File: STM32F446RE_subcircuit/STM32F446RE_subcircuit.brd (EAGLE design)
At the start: 88.6 x 55.9 mm, 47 parts, among them IC1 74AC126N, IC2 LD117AS33TR, IC3 74AC126N, IC4 74HC04N, IC5 74AC126N, U1 STM32F446RE, X1 MSTBA2, X2 32.768kHz, X3 8MHz

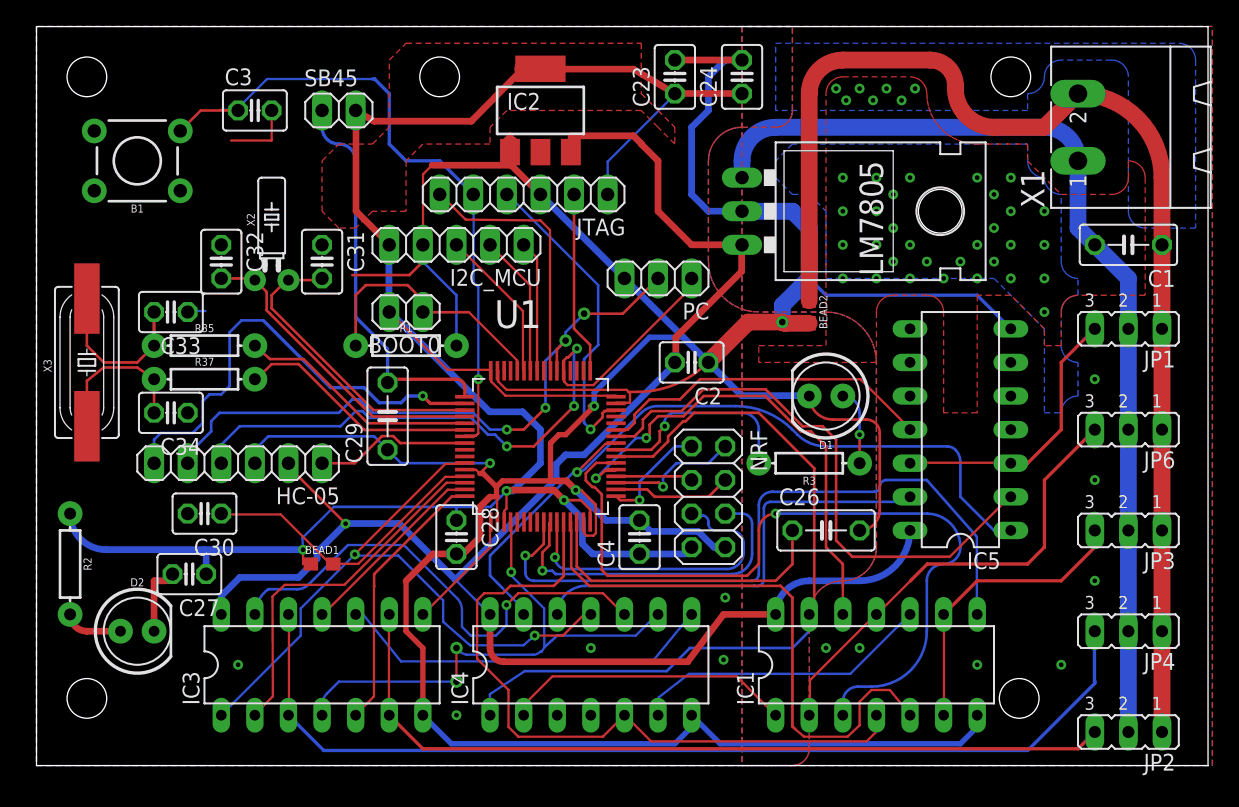
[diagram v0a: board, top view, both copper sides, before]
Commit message: Library added, Dip switch and power monitoring header was added
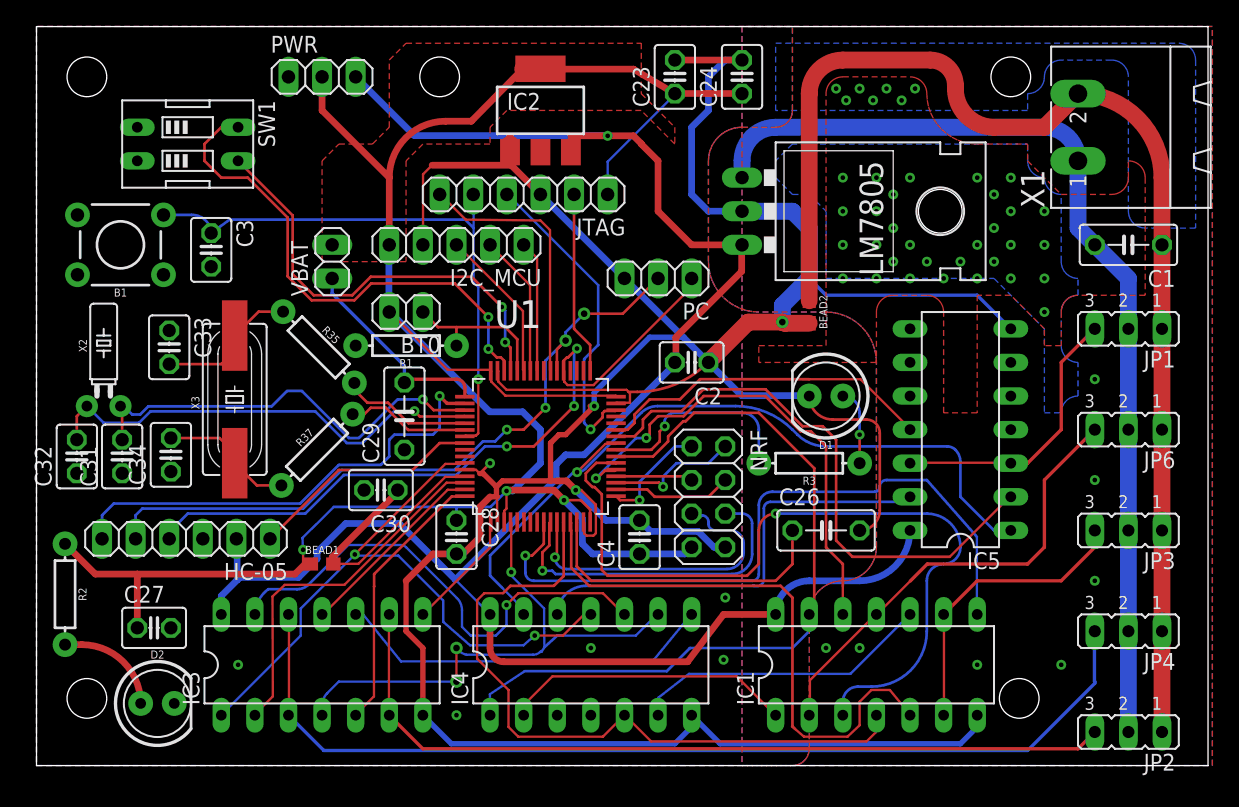
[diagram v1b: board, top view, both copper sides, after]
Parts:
- removed SB45: (no value), pinhead:1X02
- added PWR: (no value), pinhead:1X03
- added SW1: (no value), special:EDG-02
- added VBAT: (no value), pinhead:1X02
- moved C31 21.1 mm to (7.75, 38.6), turned to 90 degrees
- moved C32 18.3 mm to (4.32, 38.6), turned to 90 degrees
- moved X2 15.9 mm to (6.35, 42.4)
- moved C30 13.5 mm to (27.3, 36.1)
- moved X3 11.5 mm to (16.3, 42.9)
- moved C3 11.0 mm to (14.5, 54.2), turned to 270 degrees
- moved R37 10.0 mm to (22.5, 39.1), turned to 45 degrees
- moved R35 8.64 mm to (22.6, 46.9), turned to 315 degrees
- moved HC-05 6.94 mm to (12.6, 32.4)
- moved B1 6.48 mm to (7.62, 54.6)
- moved D2 5.67 mm to (10.4, 19.9)
- moved C27 4.86 mm to (10.2, 25.7), turned to 0 degrees
- moved C34 3.17 mm to (11.4, 38.7), turned to 90 degrees
- moved C33 2.67 mm to (11.3, 46.9), turned to 270 degrees
- moved R2 2.32 mm to (3.43, 28.2)
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- renumbered BOOT0 to BT0
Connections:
- new net SW1: SW1.3, U1.61
- new net SW2: SW1.4, U1.62
- net 5V: now also PWR.3
- net GND: now also PWR.1, SW1.1, SW1.2
- net VBAT: now also VBAT.1; no longer SB45.1
- net VDD: now also PWR.2, VBAT.2; no longer SB45.2
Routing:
- net GND: track 307.5 -> 262.0 mm
- net SW2: track 0.00 -> 39.1 mm, vias 0 -> 2
- net SW1: track 0.00 -> 33.4 mm, vias 0 -> 2
- net 5V: track 128.4 -> 146.1 mm
- net VBAT: track 29.6 -> 15.8 mm
- net N$9: track 23.7 -> 34.6 mm, vias 0 -> 1
- net N$8: track 23.2 -> 32.7 mm, vias 0 -> 1
- net N$2: track 18.4 -> 9.38 mm
- net NRST: track 53.0 -> 44.0 mm
- net N$1: track 18.3 -> 9.98 mm
- net BOOT0: track 20.0 -> 13.3 mm
- net HC05_EN: track 11.9 -> 17.7 mm
- net VDD: track 163.2 -> 168.7 mm
- net USART5_RX: track 49.3 -> 53.9 mm
- net USART5_TX: track 52.4 -> 56.0 mm
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
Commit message: final pcb iter. 1
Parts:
- renumbered IC1 to BF1, IC3 to BF2, IC4 to NOT, IC5 to BF3, JP1 to LU, JP2 to RD, JP3 to HH, JP4 to RU, JP6 to LD
